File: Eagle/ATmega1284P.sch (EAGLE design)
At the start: 32 parts, among them IC1 ATMEGA644A, IC3 LM336LP, IC4 LM1117

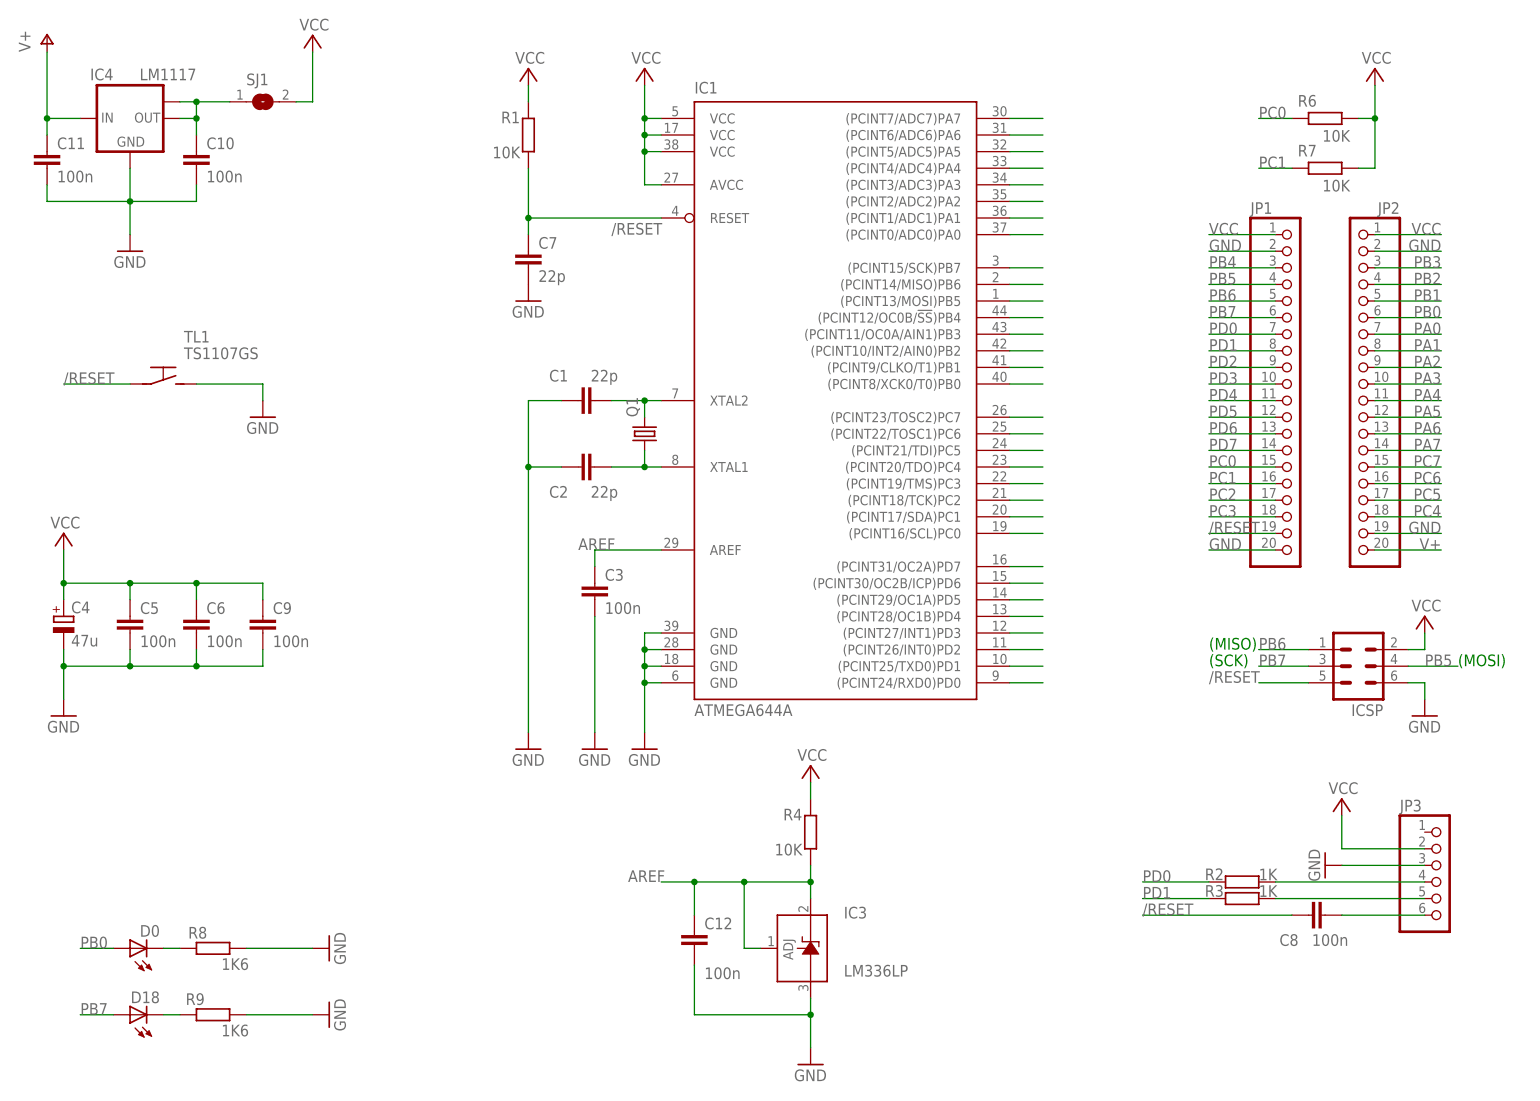
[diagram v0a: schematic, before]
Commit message: Changed voltage reference to LM4040 Changed THT crystal to SMT resonator Added a few capacitors
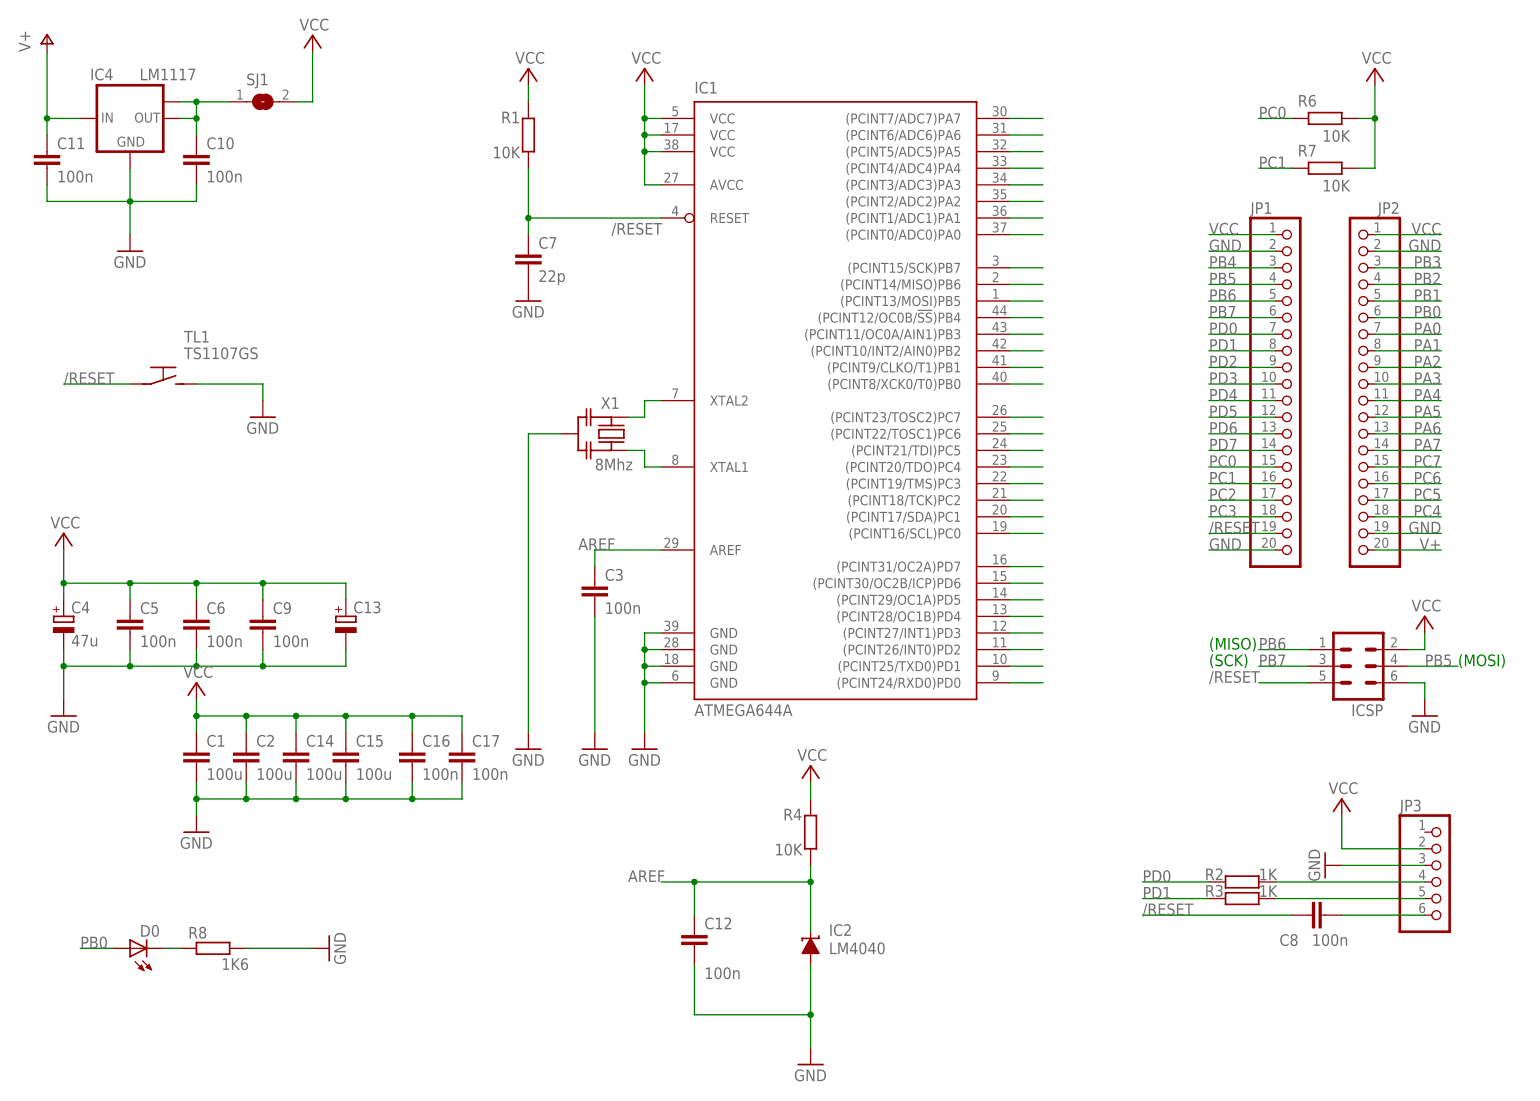
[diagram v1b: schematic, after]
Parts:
- removed D18: (no value), led:LEDCHIPLED_0805
- removed IC3: LM336LP, linear:LM336LP
- removed Q1: (no value), crystal:CRYSTALHC49S
- removed R9: 1K6, rcl:R-EU_M0805
- added C13: (no value), rcl:CPOL-EUSMCC
- added C14, C15: 100u, rcl:C-EUC1206
- added C16, C17: 100n, rcl:C-EUC0805
- added IC2: LM4040, texas:LM4041A12DBZ
- added X1: 8Mhz, SteMarie:CERMOSC-CERALOCK-CSTCE_G
- C1, C2: value 22p -> 100u; device rcl:C-EUC0805 -> rcl:C-EUC1206; TME (none) -> GRM31CR60J107ME39L
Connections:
- removed net N$31: C1.2, IC1.XTAL2, Q1.2
- removed net N$32: C2.2, IC1.XTAL1, Q1.1
- removed net N$5: D18.C, R9.2
- new net N$3: IC1.XTAL2, X1.2
- new net N$4: IC1.XTAL1, X1.1
- net AREF: now also IC2.C; no longer IC3.ADJ, IC3.C
- net GND: now also C1.2, C13.-, C14.2, C15.2, C16.1, C17.1, C2.2, IC2.A, X1.GND; no longer C1.1, C2.1, IC3.A, R9.1
- net PB7: no longer D18.A
- net VCC: now also C1.1, C13.+, C14.1, C15.1, C16.2, C17.2, C2.1
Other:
- moved on the sheet: C1, C2
